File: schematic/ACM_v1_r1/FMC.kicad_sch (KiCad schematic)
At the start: 2 parts, among them J5 DF40C-60DS-0.4V(51), J6 DF40C-60DS-0.4V(51)

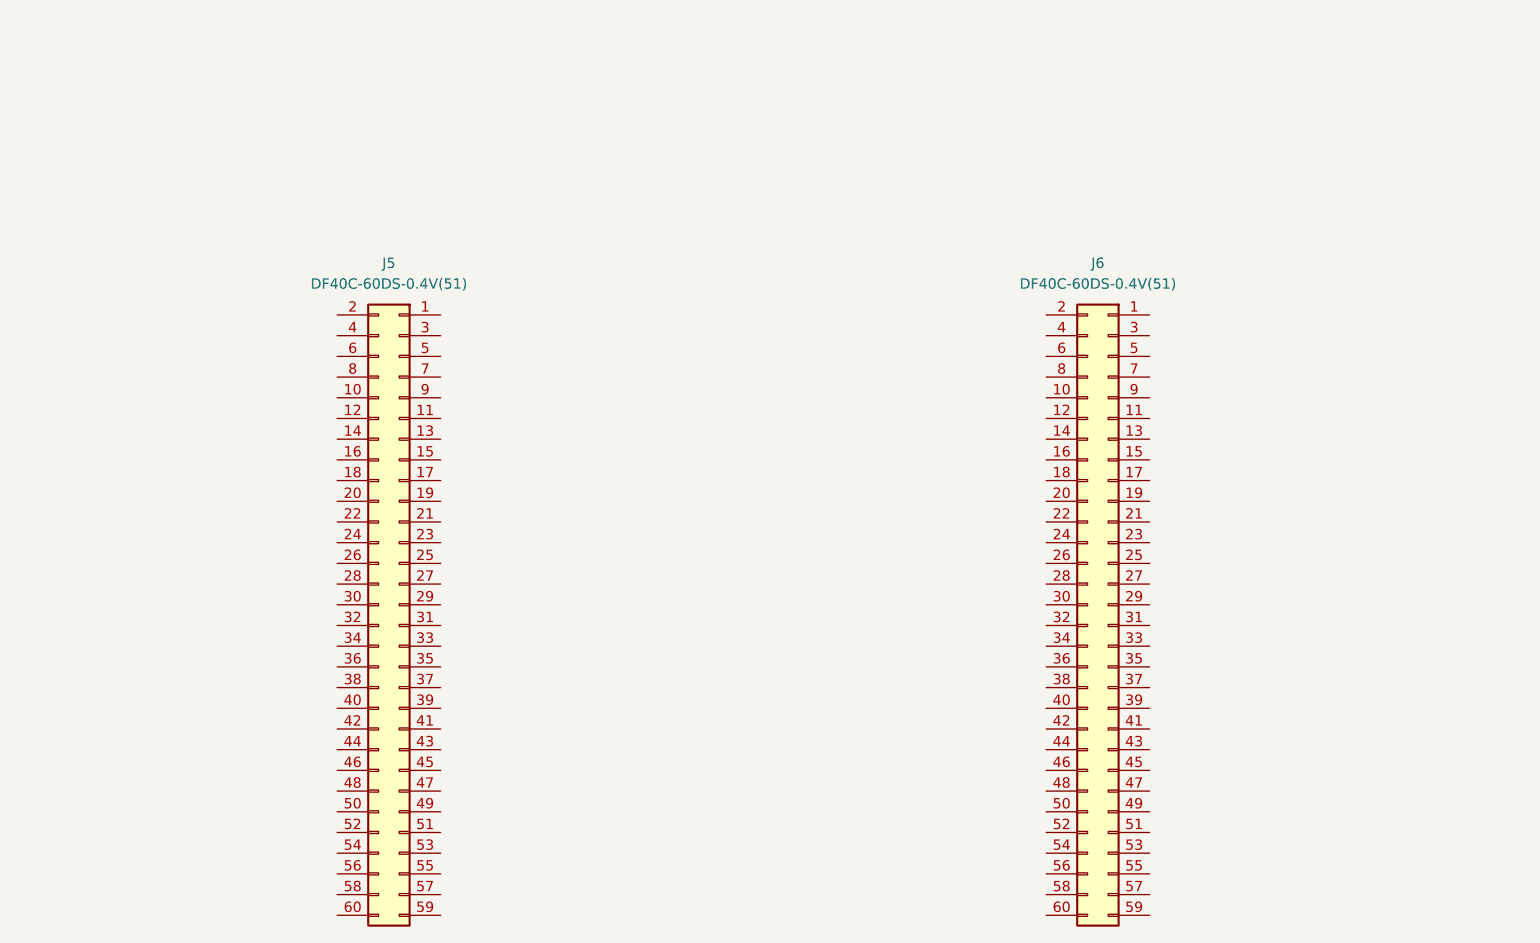
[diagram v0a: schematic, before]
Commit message: figuring out FFC traces next
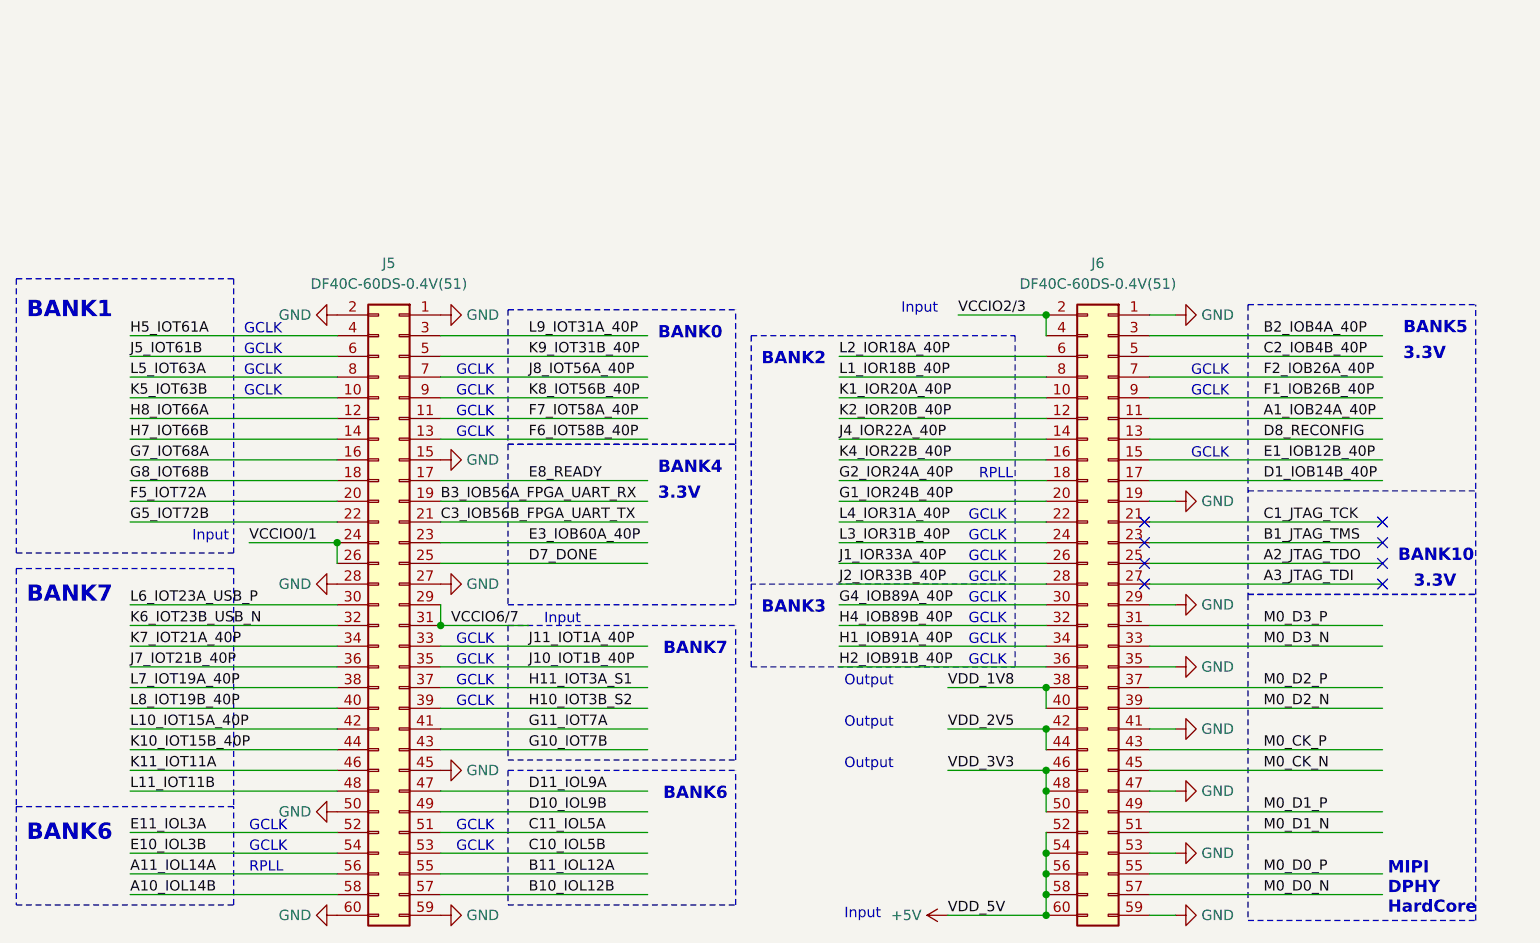
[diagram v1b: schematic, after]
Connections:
- net GND: now reaches J5.1 (Pin_1)
- net GND: now also J5.15 (Pin_15), J5.2 (Pin_2), J5.27 (Pin_27), J5.28 (Pin_28), J5.45 (Pin_45), J5.50 (Pin_50), J5.59 (Pin_59), J5.60 (Pin_60), J6.1 (Pin_1), J6.19 (Pin_19), J6.29 (Pin_29), J6.35 (Pin_35), J6.41 (Pin_41), J6.47 (Pin_47), J6.53 (Pin_53), J6.59 (Pin_59)
- net K5_IOT63B: now reaches J5.10 (Pin_10)
- net F7_IOT58A_40P: now reaches J5.11 (Pin_11)
- net H8_IOT66A: now reaches J5.12 (Pin_12)
- net F6_IOT58B_40P: now reaches J5.13 (Pin_13)
- net H7_IOT66B: now reaches J5.14 (Pin_14)
- net G7_IOT68A: now reaches J5.16 (Pin_16)
- net E8_READY: now reaches J5.17 (Pin_17)
- net G8_IOT68B: now reaches J5.18 (Pin_18)
- net B3_IOB56A_FPGA_UART_RX: now reaches J5.19 (Pin_19)
- net F5_IOT72A: now reaches J5.20 (Pin_20)
- net C3_IOB56B_FPGA_UART_TX: now reaches J5.21 (Pin_21)
- net G5_IOT72B: now reaches J5.22 (Pin_22)
- net E3_IOB60A_40P: now reaches J5.23 (Pin_23)
- net VCCIO0/1: now reaches J5.24 (Pin_24)
- net VCCIO0/1: now also J5.26 (Pin_26)
- net D7_DONE: now reaches J5.25 (Pin_25)
- net VCCIO6/7: now reaches J5.29 (Pin_29)
- net VCCIO6/7: now also J5.31 (Pin_31)
- net L9_IOT31A_40P: now reaches J5.3 (Pin_3)
- net L6_IOT23A_USB_P: now reaches J5.30 (Pin_30)
- net K6_IOT23B_USB_N: now reaches J5.32 (Pin_32)
- net J11_IOT1A_40P: now reaches J5.33 (Pin_33)
- net K7_IOT21A_40P: now reaches J5.34 (Pin_34)
- net J10_IOT1B_40P: now reaches J5.35 (Pin_35)
- net J7_IOT21B_40P: now reaches J5.36 (Pin_36)
- net H11_IOT3A_S1: now reaches J5.37 (Pin_37)
- net L7_IOT19A_40P: now reaches J5.38 (Pin_38)
- net H10_IOT3B_S2: now reaches J5.39 (Pin_39)
- net H5_IOT61A: now reaches J5.4 (Pin_4)
- net L8_IOT19B_40P: now reaches J5.40 (Pin_40)
- net G11_IOT7A: now reaches J5.41 (Pin_41)
- net L10_IOT15A_40P: now reaches J5.42 (Pin_42)
- net G10_IOT7B: now reaches J5.43 (Pin_43)
- net K10_IOT15B_40P: now reaches J5.44 (Pin_44)
- net K11_IOT11A: now reaches J5.46 (Pin_46)
- net D11_IOL9A: now reaches J5.47 (Pin_47)
- net L11_IOT11B: now reaches J5.48 (Pin_48)
- net D10_IOL9B: now reaches J5.49 (Pin_49)
- net K9_IOT31B_40P: now reaches J5.5 (Pin_5)
- net C11_IOL5A: now reaches J5.51 (Pin_51)
- net E11_IOL3A: now reaches J5.52 (Pin_52)
- net C10_IOL5B: now reaches J5.53 (Pin_53)
- net E10_IOL3B: now reaches J5.54 (Pin_54)
- net B11_IOL12A: now reaches J5.55 (Pin_55)
- net A11_IOL14A: now reaches J5.56 (Pin_56)
- net B10_IOL12B: now reaches J5.57 (Pin_57)
- net A10_IOL14B: now reaches J5.58 (Pin_58)
- net J5_IOT61B: now reaches J5.6 (Pin_6)
- net J8_IOT56A_40P: now reaches J5.7 (Pin_7)
- net L5_IOT63A: now reaches J5.8 (Pin_8)
- net K8_IOT56B_40P: now reaches J5.9 (Pin_9)
- net K1_IOR20A_40P: now reaches J6.10 (Pin_10)
- net A1_IOB24A_40P: now reaches J6.11 (Pin_11)
- net K2_IOR20B_40P: now reaches J6.12 (Pin_12)
- net D8_RECONFIG: now reaches J6.13 (Pin_13)
- net J4_IOR22A_40P: now reaches J6.14 (Pin_14)
- net E1_IOB12B_40P: now reaches J6.15 (Pin_15)
- net K4_IOR22B_40P: now reaches J6.16 (Pin_16)
- net D1_IOB14B_40P: now reaches J6.17 (Pin_17)
- net G2_IOR24A_40P: now reaches J6.18 (Pin_18)
- net VCCIO2/3: now reaches J6.2 (Pin_2)
- net VCCIO2/3: now also J6.4 (Pin_4)
- net G1_IOR24B_40P: now reaches J6.20 (Pin_20)
- net C1_JTAG_TCK: now reaches J6.21 (Pin_21)
- net L4_IOR31A_40P: now reaches J6.22 (Pin_22)
- net B1_JTAG_TMS: now reaches J6.23 (Pin_23)
- net L3_IOR31B_40P: now reaches J6.24 (Pin_24)
- net A2_JTAG_TDO: now reaches J6.25 (Pin_25)
- net J1_IOR33A_40P: now reaches J6.26 (Pin_26)
- net A3_JTAG_TDI: now reaches J6.27 (Pin_27)
- net J2_IOR33B_40P: now reaches J6.28 (Pin_28)
- net B2_IOB4A_40P: now reaches J6.3 (Pin_3)
- net G4_IOB89A_40P: now reaches J6.30 (Pin_30)
- net M0_D3_P: now reaches J6.31 (Pin_31)
- net H4_IOB89B_40P: now reaches J6.32 (Pin_32)
- net M0_D3_N: now reaches J6.33 (Pin_33)
- net H1_IOB91A_40P: now reaches J6.34 (Pin_34)
- net H2_IOB91B_40P: now reaches J6.36 (Pin_36)
- net M0_D2_P: now reaches J6.37 (Pin_37)
- net VDD_1V8: now reaches J6.38 (Pin_38)
- net VDD_1V8: now also J6.40 (Pin_40)
- net M0_D2_N: now reaches J6.39 (Pin_39)
- net VDD_2V5: now reaches J6.42 (Pin_42)
- net VDD_2V5: now also J6.44 (Pin_44)
- net M0_CK_P: now reaches J6.43 (Pin_43)
- net M0_CK_N: now reaches J6.45 (Pin_45)
- net VDD_3V3: now reaches J6.46 (Pin_46)
- net VDD_3V3: now also J6.48 (Pin_48), J6.50 (Pin_50)
- net M0_D1_P: now reaches J6.49 (Pin_49)
- net C2_IOB4B_40P: now reaches J6.5 (Pin_5)
- net M0_D1_N: now reaches J6.51 (Pin_51)
- net +5V: now reaches J6.52 (Pin_52)
- net +5V: now also J6.54 (Pin_54), J6.56 (Pin_56), J6.58 (Pin_58), J6.60 (Pin_60)
- net M0_D0_P: now reaches J6.55 (Pin_55)
- net M0_D0_N: now reaches J6.57 (Pin_57)
- net L2_IOR18A_40P: now reaches J6.6 (Pin_6)
- net F2_IOB26A_40P: now reaches J6.7 (Pin_7)
- net L1_IOR18B_40P: now reaches J6.8 (Pin_8)
- net F1_IOB26B_40P: now reaches J6.9 (Pin_9)
- no-connect marks 0 -> 8
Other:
- note added: "3.3V"
- note added: "BANK0"
- note added: "BANK1"
- note added: "BANK10"
- note added: "BANK2"
- note added: "BANK3"
- note added: "BANK4"
- note added: "BANK5"
- note added: "BANK6"
- note added: "BANK7"
- note added: "GCLK"
- note added: "Input"
- note added: "MIPI DPHY HardCore"
- note added: "Output"
- note added: "RPLL"

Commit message: getting ACM and APM schematics put together. tool for FMC pin mapping verif
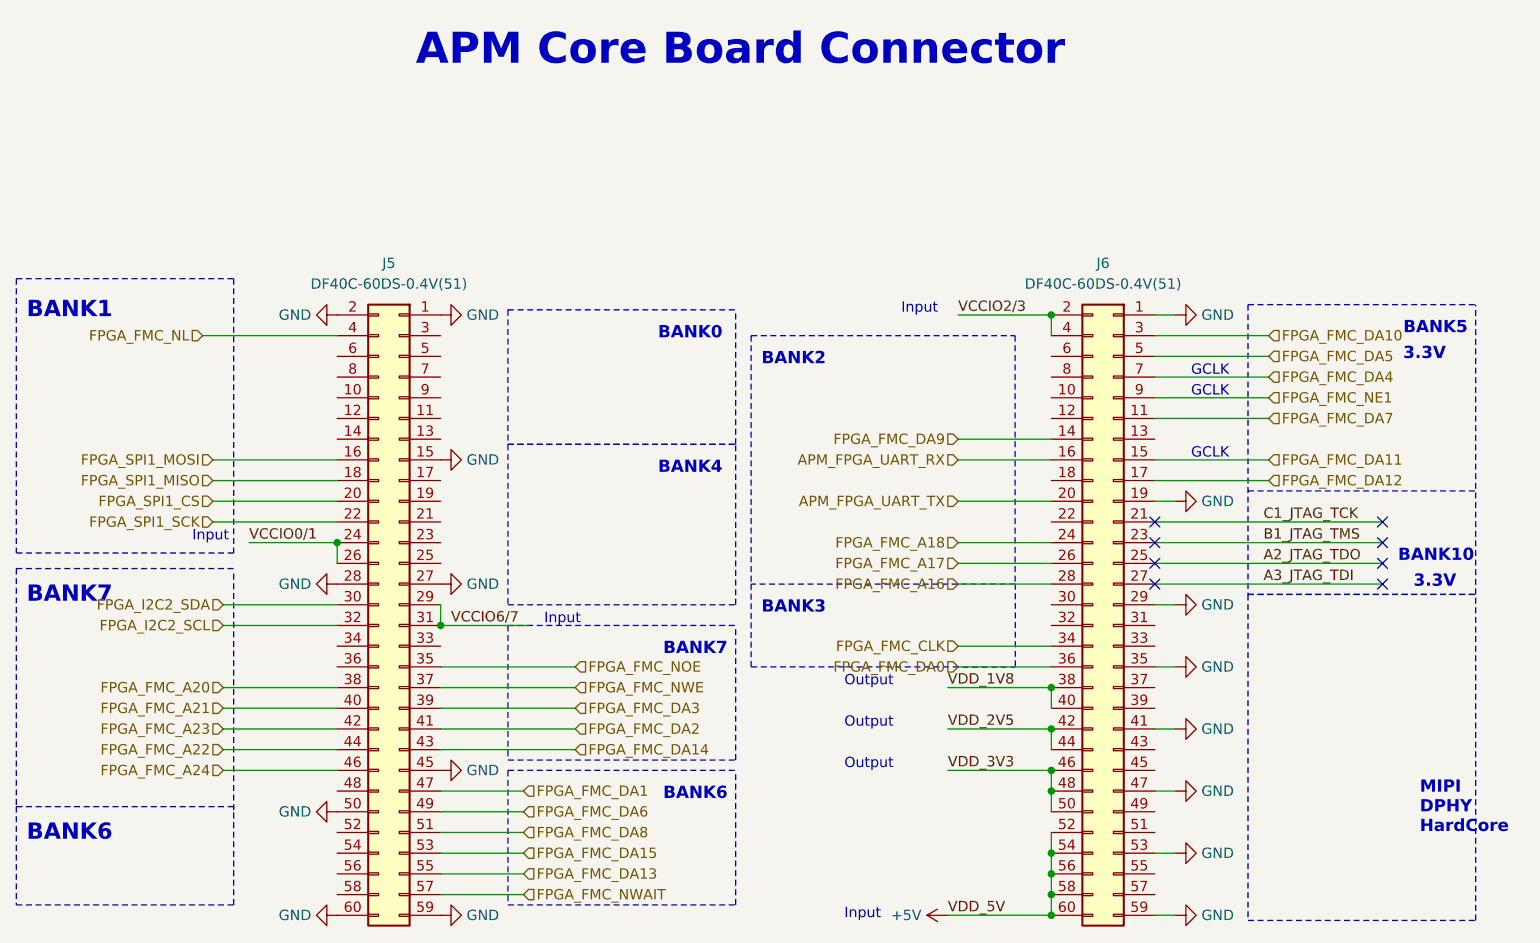
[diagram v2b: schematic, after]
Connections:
- net A10_IOL14B: no longer names the net of J5.58 (Pin_58)
- net A11_IOL14A: no longer names the net of J5.56 (Pin_56)
- net A1_IOB24A_40P renamed FPGA_FMC_DA7
- net B10_IOL12B renamed FPGA_FMC_NWAIT
- net B11_IOL12A renamed FPGA_FMC_DA13
- net B2_IOB4A_40P renamed FPGA_FMC_DA10
- net B3_IOB56A_FPGA_UART_RX: no longer names the net of J5.19 (Pin_19)
- net C10_IOL5B renamed FPGA_FMC_DA15
- net C11_IOL5A renamed FPGA_FMC_DA8
- net C2_IOB4B_40P renamed FPGA_FMC_DA5
- net C3_IOB56B_FPGA_UART_TX: no longer names the net of J5.21 (Pin_21)
- net D10_IOL9B renamed FPGA_FMC_DA6
- net D11_IOL9A renamed FPGA_FMC_DA1
- net D1_IOB14B_40P renamed FPGA_FMC_DA12
- net D7_DONE: no longer names the net of J5.25 (Pin_25)
- net D8_RECONFIG: no longer names the net of J6.13 (Pin_13)
- net E10_IOL3B: no longer names the net of J5.54 (Pin_54)
- net E11_IOL3A: no longer names the net of J5.52 (Pin_52)
- net E1_IOB12B_40P renamed FPGA_FMC_DA11
- net E3_IOB60A_40P: no longer names the net of J5.23 (Pin_23)
- net E8_READY: no longer names the net of J5.17 (Pin_17)
- net F1_IOB26B_40P renamed FPGA_FMC_NE1
- net F2_IOB26A_40P renamed FPGA_FMC_DA4
- net F5_IOT72A renamed FPGA_SPI1_CS
- net F6_IOT58B_40P: no longer names the net of J5.13 (Pin_13)
- net F7_IOT58A_40P: no longer names the net of J5.11 (Pin_11)
- net G10_IOT7B renamed FPGA_FMC_DA14
- net G11_IOT7A renamed FPGA_FMC_DA2
- net G1_IOR24B_40P renamed APM_FPGA_UART_TX
- net G2_IOR24A_40P: no longer names the net of J6.18 (Pin_18)
- net G4_IOB89A_40P: no longer names the net of J6.30 (Pin_30)
- net G5_IOT72B renamed FPGA_SPI1_SCK
- net G7_IOT68A renamed FPGA_SPI1_MOSI
- net G8_IOT68B renamed FPGA_SPI1_MISO
- net H10_IOT3B_S2 renamed FPGA_FMC_DA3
- net H11_IOT3A_S1 renamed FPGA_FMC_NWE
- net H1_IOB91A_40P renamed FPGA_FMC_CLK
- net H2_IOB91B_40P renamed FPGA_FMC_DA0
- net H4_IOB89B_40P: no longer names the net of J6.32 (Pin_32)
- net H5_IOT61A renamed FPGA_FMC_NL
- net H7_IOT66B: no longer names the net of J5.14 (Pin_14)
- net H8_IOT66A: no longer names the net of J5.12 (Pin_12)
- net J10_IOT1B_40P renamed FPGA_FMC_NOE
- net J11_IOT1A_40P: no longer names the net of J5.33 (Pin_33)
- net J1_IOR33A_40P renamed FPGA_FMC_A17
- net J2_IOR33B_40P renamed FPGA_FMC_A16
- net J4_IOR22A_40P renamed FPGA_FMC_DA9
- net J5_IOT61B: no longer names the net of J5.6 (Pin_6)
- net J7_IOT21B_40P: no longer names the net of J5.36 (Pin_36)
- net J8_IOT56A_40P: no longer names the net of J5.7 (Pin_7)
- net K10_IOT15B_40P renamed FPGA_FMC_A22
- net K11_IOT11A renamed FPGA_FMC_A24
- net K1_IOR20A_40P: no longer names the net of J6.10 (Pin_10)
- net K2_IOR20B_40P: no longer names the net of J6.12 (Pin_12)
- net K4_IOR22B_40P renamed APM_FPGA_UART_RX
- net K5_IOT63B: no longer names the net of J5.10 (Pin_10)
- net K6_IOT23B_USB_N renamed FPGA_I2C2_SCL
- net K7_IOT21A_40P: no longer names the net of J5.34 (Pin_34)
- net K8_IOT56B_40P: no longer names the net of J5.9 (Pin_9)
- net K9_IOT31B_40P: no longer names the net of J5.5 (Pin_5)
- net L10_IOT15A_40P renamed FPGA_FMC_A23
- net L11_IOT11B: no longer names the net of J5.48 (Pin_48)
- net L1_IOR18B_40P: no longer names the net of J6.8 (Pin_8)
- net L2_IOR18A_40P: no longer names the net of J6.6 (Pin_6)
- net L3_IOR31B_40P renamed FPGA_FMC_A18
- net L4_IOR31A_40P: no longer names the net of J6.22 (Pin_22)
- net L5_IOT63A: no longer names the net of J5.8 (Pin_8)
- net L6_IOT23A_USB_P renamed FPGA_I2C2_SDA
- net L7_IOT19A_40P renamed FPGA_FMC_A20
- net L8_IOT19B_40P renamed FPGA_FMC_A21
- net L9_IOT31A_40P: no longer names the net of J5.3 (Pin_3)
- net M0_CK_N: no longer names the net of J6.45 (Pin_45)
- net M0_CK_P: no longer names the net of J6.43 (Pin_43)
- net M0_D0_N: no longer names the net of J6.57 (Pin_57)
- net M0_D0_P: no longer names the net of J6.55 (Pin_55)
- net M0_D1_N: no longer names the net of J6.51 (Pin_51)
- net M0_D1_P: no longer names the net of J6.49 (Pin_49)
- net M0_D2_N: no longer names the net of J6.39 (Pin_39)
- net M0_D2_P: no longer names the net of J6.37 (Pin_37)
- net M0_D3_N: no longer names the net of J6.33 (Pin_33)
- net M0_D3_P: no longer names the net of J6.31 (Pin_31)
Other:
- note added: "APM Core Board Connector"
- note removed: "RPLL"
- moved on the sheet: J6

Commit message: seems like everything is routed? off by 1 error for I2C FPGA pins fixed?
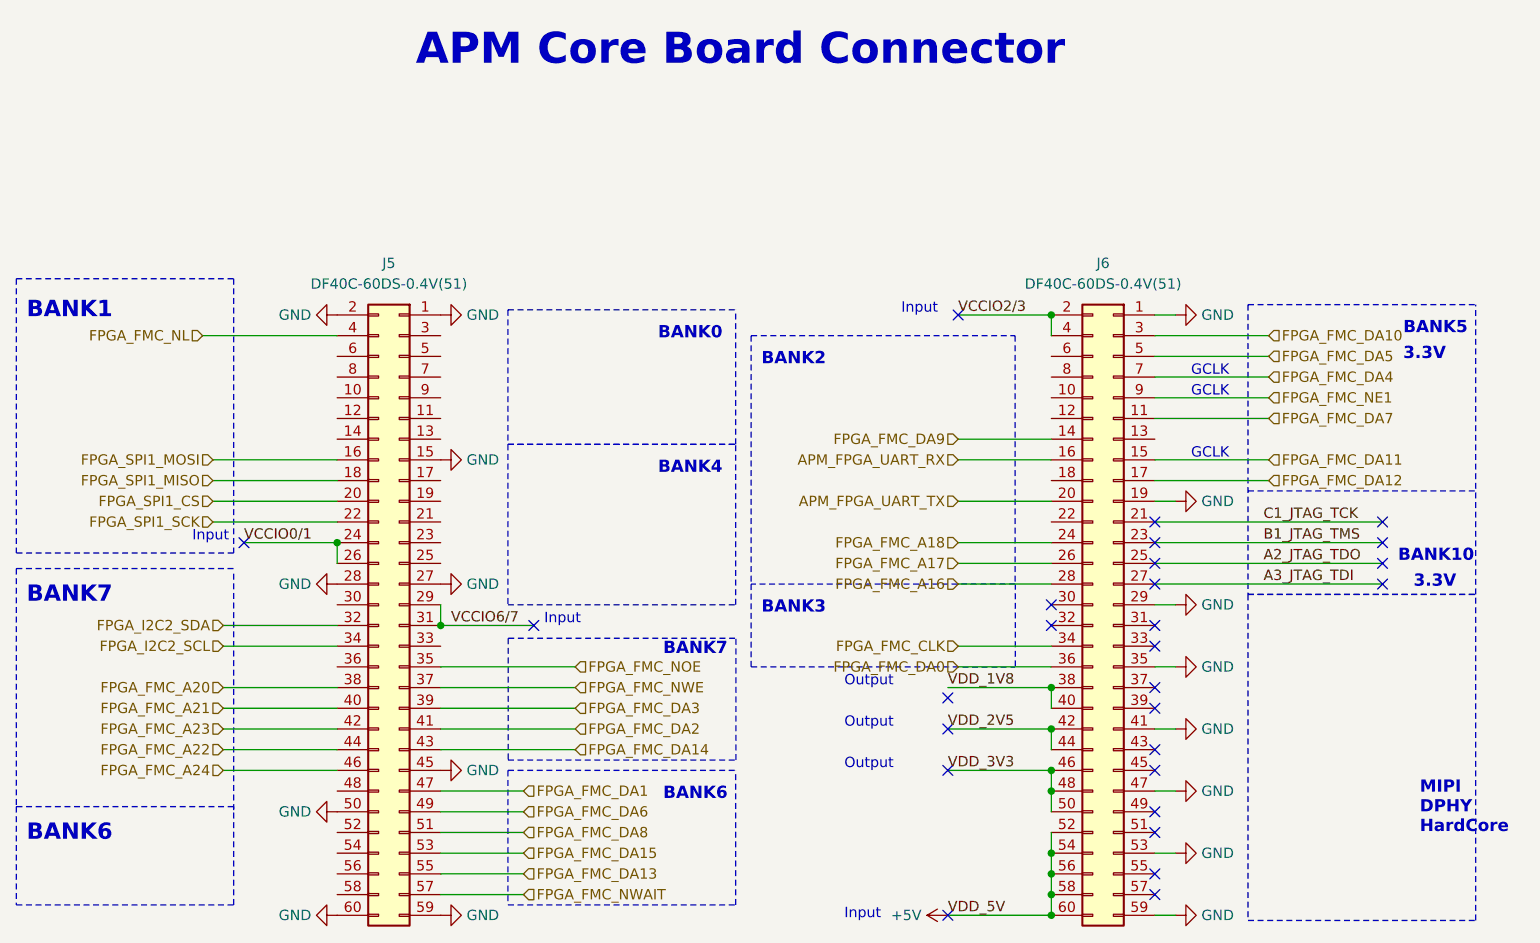
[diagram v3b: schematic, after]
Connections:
- net FPGA_I2C2_SCL: now also J5.34 (Pin_34); no longer J5.32 (Pin_32)
- net FPGA_I2C2_SDA: now also J5.32 (Pin_32); no longer J5.30 (Pin_30)
- no-connect marks 8 -> 27
